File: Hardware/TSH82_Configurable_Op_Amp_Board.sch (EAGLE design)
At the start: 33 parts, among them U1 TSH82

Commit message: Close to done, labels, layout, etc.
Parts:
- added FD1, FD2: FIDUCIAL1X2, SparkFun-Aesthetics:FIDUCIAL1X2
- added H1, H2: STAND-OFF, SparkFun-Hardware:STAND-OFF
- added LOGO1: SFE_LOGO_NAME_FLAME.2_INCH, SparkFun-Aesthetics:SFE_LOGO_NAME_FLAME.2_INCH
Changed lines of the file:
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@@
 <?xml version="1.0" encoding="utf-8"?>
 <!DOCTYPE eagle SYSTEM "eagle.dtd">
-<eagle version="9.0.1">
+<eagle version="9.1.0">
 <drawing>
 <settings>
@@
 <grid distance="0.1" unitdist="inch" unit="inch" style="lines" multiple="1" display="no" altdistance="0.01" altunitdist="inch" altunit="inch"/>
 <layers>
-<layer number="1" name="Top" color="4" fill="1" visible="yes" active="no"/>
-<layer number="2" name="Route2" color="1" fill="3" visible="yes" active="no"/>
-<layer number="15" name="Route15" color="4" fill="6" visible="yes" active="no"/>
-<layer number="16" name="Bottom" color="1" fill="1" visible="yes" active="no"/>
-<layer number="17" name="Pads" color="2" fill="1" visible="yes" active="no"/>
-<layer number="18" name="Vias" color="2" fill="1" visible="yes" active="no"/>
-<layer number="19" name="Unrouted" color="6" fill="1" visible="yes" active="no"/>
-<layer number="20" name="Dimension" color="15" fill="1" visible="yes" active="no"/>
-<layer number="21" name="tPlace" color="16" fill="1" visible="yes" active="no"/>
-<layer number="22" name="bPlace" color="14" fill="1" visible="yes" active="no"/>
-<layer number="23" name="tOrigins" color="15" fill="1" visible="yes" active="no"/>
-<layer number="24" name="bOrigins" color="15" fill="1" visible="yes" active="no"/>
-<layer number="25" name="tNames" color="7" fill="1" visible="yes" active="no"/>
-<layer number="26" name="bNames" color="7" fill="1" visible="yes" active="no"/>
-<layer number="27" name="tValues" color="7" fill="1" visible="yes" active="no"/>
-<layer number="28" name="bValues" color="7" fill="1" visible="yes" active="no"/>
+<layer number="1" name="Top" color="4" fill="1" visible="no" active="no"/>
+<layer number="2" name="Route2" color="1" fill="3" visible="no" active="no"/>
+<layer number="15" name="Route15" color="4" fill="6" visible="no" active="no"/>
+<layer number="16" name="Bottom" color="1" fill="1" visible="no" active="no"/>
+<layer number="17" name="Pads" color="2" fill="1" visible="no" active="no"/>
+<layer number="18" name="Vias" color="2" fill="1" visible="no" active="no"/>
+<layer number="19" name="Unrouted" color="6" fill="1" visible="no" active="no"/>
+<layer number="20" name="Dimension" color="15" fill="1" visible="no" active="no"/>
+<layer number="21" name="tPlace" color="16" fill="1" visible="no" active="no"/>
+<layer number="22" name="bPlace" color="14" fill="1" visible="no" active="no"/>
+<layer number="23" name="tOrigins" color="15" fill="1" visible="no" active="no"/>
+<layer number="24" name="bOrigins" color="15" fill="1" visible="no" active="no"/>
+<layer number="25" name="tNames" color="7" fill="1" visible="no" active="no"/>
+<layer number="26" name="bNames" color="7" fill="1" visible="no" active="no"/>
+<layer number="27" name="tValues" color="7" fill="1" visible="no" active="no"/>
+<layer number="28" name="bValues" color="7" fill="1" visible="no" active="no"/>
 <layer number="29" name="tStop" color="7" fill="3" visible="no" active="no"/>
 <layer number="30" name="bStop" color="7" fill="6" visible="no" active="no"/>
@@
 <layer number="35" name="tGlue" color="7" fill="4" visible="no" active="no"/>
 <layer number="36" name="bGlue" color="7" fill="5" visible="no" active="no"/>
-<layer number="37" name="tTest" color="7" fill="1" visible="yes" active="no"/>
-<layer number="38" name="bTest" color="7" fill="1" visible="yes" active="no"/>
+<layer number="37" name="tTest" color="7" fill="1" visible="no" active="no"/>
+<layer number="38" name="bTest" color="7" fill="1" visible="no" active="no"/>
 <layer number="39" name="tKeepout" color="4" fill="11" visible="no" active="no"/>
 <layer number="40" name="bKeepout" color="1" fill="11" visible="no" active="no"/>
@@
 <layer number="44" name="Drills" color="7" fill="1" visible="no" active="no"/>
 <layer number="45" name="Holes" color="7" fill="1" visible="no" active="no"/>
-<layer number="46" name="Milling" color="3" fill="1" visible="yes" active="no"/>
-<layer number="47" name="Measures" color="7" fill="1" visible="yes" active="no"/>
-<layer number="48" name="Document" color="7" fill="1" visible="yes" active="no"/>
-<layer number="49" name="Reference" color="7" fill="1" visible="yes" active="no"/>
-<layer number="50" name="dxf" color="7" fill="1" visible="yes" active="no"/>
-<layer number="51" name="tDocu" color="6" fill="1" visible="yes" active="no"/>
-<layer number="52" name="bDocu" color="7" fill="1" visible="yes" active="no"/>
-<layer number="53" name="tGND_GNDA" color="7" fill="9" visible="yes" active="no"/>
-<layer number="54" name="bGND_GNDA" color="1" fill="9" visible="yes" active="no"/>
-<layer number="56" name="wert" color="7" fill="1" visible="yes" active="no"/>
-<layer number="57" name="tCAD" color="7" fill="1" visible="yes" active="no"/>
-<layer number="59" name="tCarbon" color="7" fill="1" visible="yes" active="no"/>
-<layer number="60" name="bCarbon" color="7" fill="1" visible="yes" active="no"/>
+<layer number="46" name="Milling" color="3" fill="1" visible="no" active="no"/>
+<layer number="47" name="Measures" color="7" fill="1" visible="no" active="no"/>
+<layer number="48" name="Document" color="7" fill="1" visible="no" active="no"/>
+<layer number="49" name="Reference" color="7" fill="1" visible="no" active="no"/>
+<layer number="50" name="dxf" color="7" fill="1" visible="no" active="no"/>
+<layer number="51" name="tDocu" color="6" fill="1" visible="no" active="no"/>
+<layer number="52" name="bDocu" color="7" fill="1" visible="no" active="no"/>
+<layer number="53" name="tGND_GNDA" color="7" fill="9" visible="no" active="no"/>
+<layer number="54" name="bGND_GNDA" color="1" fill="9" visible="no" active="no"/>
+<layer number="56" name="wert" color="7" fill="1" visible="no" active="no"/>
+<layer number="57" name="tCAD" color="7" fill="1" visible="no" active="no"/>
+<layer number="59" name="tCarbon" color="7" fill="1" visible="no" active="no"/>
+<layer number="60" name="bCarbon" color="7" fill="1" visible="no" active="no"/>
 <layer number="88" name="SimResults" color="9" fill="1" visible="yes" active="yes"/>
 <layer number="89" name="SimProbes" color="9" fill="1" visible="yes" active="yes"/>
@@
 <part name="C3" library="SparkFun-Capacitors" deviceset="10UF-POLAR" device="-EIA3216-16V-10%(TANT)" value="10uF"/>
 <part name="C10" library="SparkFun-Capacitors" deviceset="0.1UF" device="-0603-25V-(+80/-20%)" value="0.1uF"/>
+<part name="LOGO1" library="SparkFun-Aesthetics" deviceset="SFE_LOGO_NAME_FLAME" device=".2_INCH"/>
+<part name="H1" library="SparkFun-Hardware" deviceset="STAND-OFF" device=""/>
+<part name="H2" library="SparkFun-Hardware" deviceset="STAND-OFF" device=""/>
+<part name="FD1" library="SparkFun-Aesthetics" deviceset="FIDUCIAL" device="1X2"/>
+<part name="FD2" library="SparkFun-Aesthetics" deviceset="FIDUCIAL" device="1X2"/>
 </parts>
 <sheets>
@@
 <instance part="C3" gate="G$1" x="106.68" y="45.72"/>
 <instance part="C10" gate="G$1" x="119.38" y="43.18"/>
+<instance part="LOGO1" gate="G$1" x="167.64" y="48.26"/>
+<instance part="H1" gate="G$1" x="233.68" y="40.64"/>
+<instance part="H2" gate="G$1" x="238.76" y="40.64"/>
+<instance part="FD1" gate="G$1" x="228.6" y="40.64"/>
+<instance part="FD2" gate="G$1" x="223.52" y="40.64"/>
 </instances>
 <busses>

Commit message: Ready for review.
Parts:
- removed FD1, FD2: FIDUCIAL1X2, SparkFun-Aesthetics:FIDUCIAL1X2
- added LOGO2: SFE_LOGO_NAME_FLAME.1_INCH, SparkFun-Aesthetics:SFE_LOGO_NAME_FLAME.1_INCH
- added LOGO3: OSHW-LOGOS, SparkFun-Aesthetics:OSHW-LOGOS
- LOGO1: value SFE_LOGO_NAME_FLAME.2_INCH -> SFE_LOGO_FLAME.2_INCH; device SparkFun-Aesthetics:SFE_LOGO_NAME_FLAME.2_INCH -> SparkFun-Aesthetics:SFE_LOGO_FLAME.2_INCH
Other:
- note added: "+VCC - (-VEE) = 4.5V-12V"
- note added: "v01"
- moved on the sheet: C1, C2, R1, R2
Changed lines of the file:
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@@
 <part name="C3" library="SparkFun-Capacitors" deviceset="10UF-POLAR" device="-EIA3216-16V-10%(TANT)" value="10uF"/>
 <part name="C10" library="SparkFun-Capacitors" deviceset="0.1UF" device="-0603-25V-(+80/-20%)" value="0.1uF"/>
-<part name="LOGO1" library="SparkFun-Aesthetics" deviceset="SFE_LOGO_NAME_FLAME" device=".2_INCH"/>
 <part name="H1" library="SparkFun-Hardware" deviceset="STAND-OFF" device=""/>
 <part name="H2" library="SparkFun-Hardware" deviceset="STAND-OFF" device=""/>
-<part name="FD1" library="SparkFun-Aesthetics" deviceset="FIDUCIAL" device="1X2"/>
-<part name="FD2" library="SparkFun-Aesthetics" deviceset="FIDUCIAL" device="1X2"/>
+<part name="LOGO1" library="SparkFun-Aesthetics" deviceset="SFE_LOGO_FLAME" device=".2_INCH"/>
+<part name="LOGO2" library="SparkFun-Aesthetics" deviceset="SFE_LOGO_NAME_FLAME" device=".1_INCH"/>
+<part name="LOGO3" library="SparkFun-Aesthetics" deviceset="OSHW-LOGO" device="S"/>
 </parts>
 <sheets>
@@
 <wire x1="0" y1="81.28" x2="124.46" y2="81.28" width="0.1524" layer="97" style="shortdash"/>
 <wire x1="124.46" y1="81.28" x2="147.32" y2="81.28" width="0.1524" layer="97" style="shortdash"/>
-<wire x1="147.32" y1="81.28" x2="248.92" y2="81.28" width="0.1524" layer="97" style="shortdash"/>
 <wire x1="124.46" y1="185.42" x2="124.46" y2="81.28" width="0.1524" layer="97" style="shortdash"/>
 <wire x1="147.32" y1="35.56" x2="147.32" y2="81.28" width="0.1524" layer="97" style="shortdash"/>
@@
 <text x="20.32" y="20.32" size="2.54" layer="94" font="vector">Connector</text>
 <text x="81.28" y="15.24" size="2.54" layer="94" font="vector">Power and Reference</text>
+<text x="238.76" y="7.62" size="2.54" layer="94">v01</text>
+<text x="9.144" y="14.478" size="2.54" layer="94" font="vector">+VCC - (-VEE) = 4.5V-12V</text>
 </plain>
 <instances>
@@
 <instance part="FRAME1" gate="G$1" x="0" y="0"/>
 <instance part="FRAME1" gate="V" x="147.32" y="0"/>
-<instance part="R1" gate="G$1" x="68.58" y="53.34" smashed="yes" rot="R90">
-<attribute name="NAME" x="67.056" y="53.34" size="1.778" layer="95" font="vector" rot="R90" align="bottom-center"/>
-<attribute name="VALUE" x="70.104" y="53.34" size="1.778" layer="96" font="vector" rot="R90" align="top-center"/>
-</instance>
-<instance part="R2" gate="G$1" x="68.58" y="38.1" smashed="yes" rot="R90">
-<attribute name="NAME" x="67.056" y="38.1" size="1.778" layer="95" font="vector" rot="R90" align="bottom-center"/>
-<attribute name="VALUE" x="70.104" y="38.1" size="1.778" layer="96" font="vector" rot="R90" align="top-center"/>
-</instance>
-<instance part="C2" gate="G$1" x="93.98" y="35.56" smashed="yes">
-<attribute name="NAME" x="95.504" y="38.481" size="1.778" layer="95" font="vector"/>
-<attribute name="VALUE" x="95.504" y="33.401" size="1.778" layer="96" font="vector"/>
+<instance part="R1" gate="G$1" x="60.96" y="53.34" smashed="yes" rot="R90">
+<attribute name="NAME" x="59.436" y="53.34" size="1.778" layer="95" font="vector" rot="R90" align="bottom-center"/>
+<attribute name="VALUE" x="62.484" y="53.34" size="1.778" layer="96" font="vector" rot="R90" align="top-center"/>
+</instance>
+<instance part="R2" gate="G$1" x="60.96" y="38.1" smashed="yes" rot="R90">
+<attribute name="NAME" x="59.436" y="38.1" size="1.778" layer="95" font="vector" rot="R90" align="bottom-center"/>
+<attribute name="VALUE" x="62.484" y="38.1" size="1.778" layer="96" font="vector" rot="R90" align="top-center"/>
+</instance>
+<instance part="C2" gate="G$1" x="86.36" y="35.56" smashed="yes">
+<attribute name="NAME" x="87.884" y="38.481" size="1.778" layer="95" font="vector"/>
+<attribute name="VALUE" x="87.884" y="33.401" size="1.778" layer="96" font="vector"/>
 </instance>
 <instance part="-VEE" gate="G$2" x="99.06" y="25.4" smashed="yes">
@@
 <attribute name="NAME" x="198.12" y="116.84" size="1.778" layer="95" font="vector" rot="R270"/>
 </instance>
-<instance part="C1" gate="G$1" x="81.28" y="38.1"/>
+<instance part="C1" gate="G$1" x="73.66" y="38.1"/>
 <instance part="C3" gate="G$1" x="106.68" y="45.72"/>
 <instance part="C10" gate="G$1" x="119.38" y="43.18"/>
-<instance part="LOGO1" gate="G$1" x="167.64" y="48.26"/>
-<instance part="H1" gate="G$1" x="233.68" y="40.64"/>
-<instance part="H2" gate="G$1" x="238.76" y="40.64"/>
-<instance part="FD1" gate="G$1" x="228.6" y="40.64"/>
-<instance part="FD2" gate="G$1" x="223.52" y="40.64"/>
+<instance part="H1" gate="G$1" x="241.808" y="40.894"/>
+<instance part="H2" gate="G$1" x="245.618" y="40.894"/>
+<instance part="LOGO1" gate="G$1" x="182.626" y="48.26"/>
+<instance part="LOGO2" gate="G$1" x="150.114" y="35.814"/>
+<instance part="LOGO3" gate="G$1" x="223.012" y="49.022"/>
 </instances>
 <busses>
@@
 <pinref part="R1" gate="G$1" pin="1"/>
 <pinref part="R2" gate="G$1" pin="2"/>
-<wire x1="68.58" y1="48.26" x2="68.58" y2="45.72" width="0.1524" layer="91"/>
-<wire x1="68.58" y1="45.72" x2="68.58" y2="43.18" width="0.1524" layer="91"/>
-<wire x1="81.28" y1="40.64" x2="81.28" y2="45.72" width="0.1524" layer="91"/>
-<wire x1="81.28" y1="45.72" x2="68.58" y2="45.72" width="0.1524" layer="91"/>
+<wire x1="60.96" y1="48.26" x2="60.96" y2="45.72" width="0.1524" layer="91"/>
+<wire x1="60.96" y1="45.72" x2="60.96" y2="43.18" width="0.1524" layer="91"/>
+<wire x1="73.66" y1="40.64" x2="73.66" y2="45.72" width="0.1524" layer="91"/>
+<wire x1="73.66" y1="45.72" x2="60.96" y2="45.72" width="0.1524" layer="91"/>
 <pinref part="C2" gate="G$1" pin="1"/>
-<wire x1="93.98" y1="40.64" x2="93.98" y2="45.72" width="0.1524" layer="91"/>
-<wire x1="93.98" y1="45.72" x2="81.28" y2="45.72" width="0.1524" layer="91"/>
-<junction x="68.58" y="45.72"/>
-<junction x="81.28" y="45.72"/>
-<label x="60.96" y="45.72" size="1.778" layer="95" rot="R180" xref="yes"/>
-<wire x1="60.96" y1="45.72" x2="68.58" y2="45.72" width="0.1524" layer="91"/>
+<wire x1="86.36" y1="40.64" x2="86.36" y2="45.72" width="0.1524" layer="91"/>
+<wire x1="86.36" y1="45.72" x2="73.66" y2="45.72" width="0.1524" layer="91"/>
+<junction x="60.96" y="45.72"/>
+<junction x="73.66" y="45.72"/>
+<label x="91.44" y="45.72" size="1.778" layer="95" xref="yes"/>
 <pinref part="C1" gate="G$1" pin="+"/>
+<wire x1="86.36" y1="45.72" x2="91.44" y2="45.72" width="0.1524" layer="91"/>
 </segment>
 <segment>
@@
 <segment>
 <pinref part="R2" gate="G$1" pin="1"/>
-<wire x1="68.58" y1="33.02" x2="68.58" y2="30.48" width="0.1524" layer="91"/>
-<wire x1="68.58" y1="30.48" x2="81.28" y2="30.48" width="0.1524" layer="91"/>
-<wire x1="81.28" y1="30.48" x2="93.98" y2="30.48" width="0.1524" layer="91"/>
-<wire x1="93.98" y1="30.48" x2="99.06" y2="30.48" width="0.1524" layer="91"/>
+<wire x1="60.96" y1="33.02" x2="60.96" y2="30.48" width="0.1524" layer="91"/>
+<wire x1="60.96" y1="30.48" x2="73.66" y2="30.48" width="0.1524" layer="91"/>
+<wire x1="73.66" y1="30.48" x2="86.36" y2="30.48" width="0.1524" layer="91"/>
+<wire x1="86.36" y1="30.48" x2="99.06" y2="30.48" width="0.1524" layer="91"/>
 <wire x1="99.06" y1="30.48" x2="106.68" y2="30.48" width="0.1524" layer="91"/>
 <wire x1="106.68" y1="30.48" x2="106.68" y2="40.64" width="0.1524" layer="91"/>
-<wire x1="81.28" y1="33.02" x2="81.28" y2="30.48" width="0.1524" layer="91"/>
+<wire x1="73.66" y1="33.02" x2="73.66" y2="30.48" width="0.1524" layer="91"/>
 <pinref part="C2" gate="G$1" pin="2"/>
-<wire x1="93.98" y1="33.02" x2="93.98" y2="30.48" width="0.1524" layer="91"/>
-<junction x="93.98" y="30.48"/>
-<junction x="81.28" y="30.48"/>
+<wire x1="86.36" y1="33.02" x2="86.36" y2="30.48" width="0.1524" layer="91"/>
+<junction x="86.36" y="30.48"/>
+<junction x="73.66" y="30.48"/>
 <wire x1="132.08" y1="35.56" x2="132.08" y2="30.48" width="0.1524" layer="91"/>
 <wire x1="132.08" y1="30.48" x2="119.38" y2="30.48" width="0.1524" layer="91"/>
@@
 <segment>
 <pinref part="R1" gate="G$1" pin="2"/>
-<wire x1="68.58" y1="58.42" x2="68.58" y2="60.96" width="0.1524" layer="91"/>
-<wire x1="68.58" y1="60.96" x2="99.06" y2="60.96" width="0.1524" layer="91"/>
+<wire x1="60.96" y1="58.42" x2="60.96" y2="60.96" width="0.1524" layer="91"/>
+<wire x1="60.96" y1="60.96" x2="99.06" y2="60.96" width="0.1524" layer="91"/>
 <wire x1="99.06" y1="60.96" x2="106.68" y2="60.96" width="0.1524" layer="91"/>
 <wire x1="106.68" y1="60.96" x2="106.68" y2="48.26" width="0.1524" layer="91"/>

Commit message: Changes post design review.
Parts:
- added FD1, FD2: FIDUCIALUFIDUCIAL, SparkFun-Aesthetics:FIDUCIALUFIDUCIAL
- J1: device SparkFun-Connectors:CONN_09 -> SparkFun-Connectors:CONN_09NO_SILK
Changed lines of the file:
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@@
 <layer number="18" name="Vias" color="2" fill="1" visible="no" active="no"/>
 <layer number="19" name="Unrouted" color="6" fill="1" visible="no" active="no"/>
-<layer number="20" name="Dimension" color="15" fill="1" visible="no" active="no"/>
-<layer number="21" name="tPlace" color="16" fill="1" visible="no" active="no"/>
-<layer number="22" name="bPlace" color="14" fill="1" visible="no" active="no"/>
+<layer number="20" name="Dimension" color="24" fill="1" visible="no" active="no"/>
+<layer number="21" name="tPlace" color="7" fill="1" visible="no" active="no"/>
+<layer number="22" name="bPlace" color="7" fill="1" visible="no" active="no"/>
 <layer number="23" name="tOrigins" color="15" fill="1" visible="no" active="no"/>
 <layer number="24" name="bOrigins" color="15" fill="1" visible="no" active="no"/>
@@
 <layer number="49" name="Reference" color="7" fill="1" visible="no" active="no"/>
 <layer number="50" name="dxf" color="7" fill="1" visible="no" active="no"/>
-<layer number="51" name="tDocu" color="6" fill="1" visible="no" active="no"/>
+<layer number="51" name="tDocu" color="7" fill="1" visible="no" active="no"/>
 <layer number="52" name="bDocu" color="7" fill="1" visible="no" active="no"/>
 <layer number="53" name="tGND_GNDA" color="7" fill="9" visible="no" active="no"/>
@@
 </classes>
 <parts>
-<part name="J1" library="SparkFun-Connectors" deviceset="CONN_09" device=""/>
+<part name="J1" library="SparkFun-Connectors" deviceset="CONN_09" device="NO_SILK"/>
 <part name="FRAME1" library="SparkFun-Aesthetics" deviceset="FRAME-LETTER" device=""/>
 <part name="R1" library="SparkFun-Resistors" deviceset="2.2KOHM" device="-0603-1/10W-1%" value="2.2k"/>
@@
 <part name="LOGO2" library="SparkFun-Aesthetics" deviceset="SFE_LOGO_NAME_FLAME" device=".1_INCH"/>
 <part name="LOGO3" library="SparkFun-Aesthetics" deviceset="OSHW-LOGO" device="S"/>
+<part name="FD1" library="SparkFun-Aesthetics" deviceset="FIDUCIAL" device="UFIDUCIAL"/>
+<part name="FD2" library="SparkFun-Aesthetics" deviceset="FIDUCIAL" device="UFIDUCIAL"/>
 </parts>
 <sheets>
@@
 <instance part="C3" gate="G$1" x="106.68" y="45.72"/>
 <instance part="C10" gate="G$1" x="119.38" y="43.18"/>
-<instance part="H1" gate="G$1" x="241.808" y="40.894"/>
-<instance part="H2" gate="G$1" x="245.618" y="40.894"/>
+<instance part="H1" gate="G$1" x="241.808" y="45.974"/>
+<instance part="H2" gate="G$1" x="245.618" y="45.974"/>
 <instance part="LOGO1" gate="G$1" x="182.626" y="48.26"/>
 <instance part="LOGO2" gate="G$1" x="150.114" y="35.814"/>
 <instance part="LOGO3" gate="G$1" x="223.012" y="49.022"/>
+<instance part="FD1" gate="G$1" x="241.808" y="42.418"/>
+<instance part="FD2" gate="G$1" x="245.618" y="42.418"/>
 </instances>
 <busses>
@@
 <pinref part="C1" gate="G$1" pin="+"/>
 <wire x1="86.36" y1="45.72" x2="91.44" y2="45.72" width="0.1524" layer="91"/>
+<junction x="86.36" y="45.72"/>
 </segment>
 <segment>
@@
 <wire x1="78.74" y1="157.48" x2="73.66" y2="157.48" width="0.1524" layer="91"/>
 <wire x1="73.66" y1="157.48" x2="73.66" y2="149.86" width="0.1524" layer="91"/>
+<junction x="73.66" y="149.86"/>
 </segment>
 </net>
@@
 <wire x1="93.98" y1="139.7" x2="101.6" y2="139.7" width="0.1524" layer="91"/>
 <label x="101.6" y="139.7" size="1.778" layer="95" xref="yes"/>
-</segment>
-<segment>
+<junction x="93.98" y="149.86"/>
+<junction x="93.98" y="139.7"/>
+</segment>
+<segment>

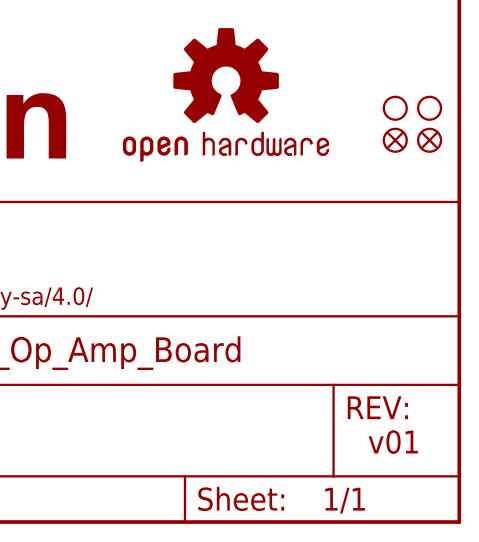
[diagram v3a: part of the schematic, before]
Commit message: Add bottom fiducials, move a trace, increment version, remove extra files.
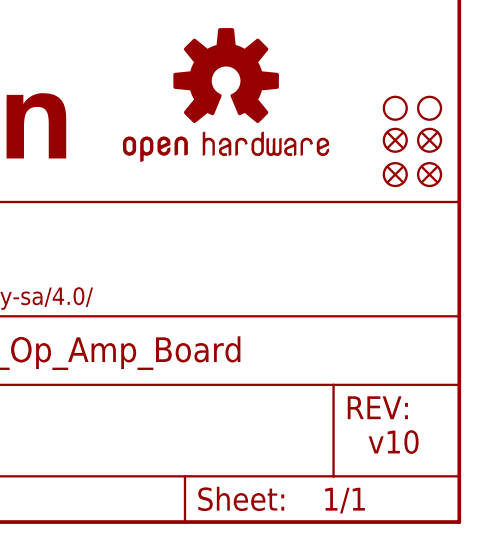
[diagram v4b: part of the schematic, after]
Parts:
- added FD3, FD4: FIDUCIALUFIDUCIAL, SparkFun-Aesthetics:FIDUCIALUFIDUCIAL
- U1: device pete:TSH82 -> SparkFun-IC-Amplifiers:TSH82
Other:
- note added: "v10"
- note removed: "v01"
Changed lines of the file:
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@@
 <part name="SUPPLY3" library="SparkFun-PowerSymbols" deviceset="VCC" device="" value="+VCC"/>
 <part name="SUPPLY4" library="SparkFun-PowerSymbols" deviceset="VNEG" device="" value="-VEE"/>
-<part name="U1" library="pete" deviceset="TSH82" device=""/>
+<part name="U1" library="SparkFun-IC-Amplifiers" deviceset="TSH82" device=""/>
 <part name="R3" library="SparkFun-Resistors" deviceset="10KOHM" device="-0603-1/10W-1%" value="10k"/>
 <part name="R4" library="SparkFun-Resistors" deviceset="10KOHM" device="-0603-1/10W-1%" value="10k"/>
@@
 <part name="FD1" library="SparkFun-Aesthetics" deviceset="FIDUCIAL" device="UFIDUCIAL"/>
 <part name="FD2" library="SparkFun-Aesthetics" deviceset="FIDUCIAL" device="UFIDUCIAL"/>
+<part name="FD3" library="SparkFun-Aesthetics" deviceset="FIDUCIAL" device="UFIDUCIAL"/>
+<part name="FD4" library="SparkFun-Aesthetics" deviceset="FIDUCIAL" device="UFIDUCIAL"/>
 </parts>
 <sheets>
@@
 <text x="20.32" y="20.32" size="2.54" layer="94" font="vector">Connector</text>
 <text x="81.28" y="15.24" size="2.54" layer="94" font="vector">Power and Reference</text>
-<text x="238.76" y="7.62" size="2.54" layer="94">v01</text>
+<text x="238.76" y="7.62" size="2.54" layer="94">v10</text>
 <text x="9.144" y="14.478" size="2.54" layer="94" font="vector">+VCC - (-VEE) = 4.5V-12V</text>
 </plain>
@@
 <instance part="FD1" gate="G$1" x="241.808" y="42.418"/>
 <instance part="FD2" gate="G$1" x="245.618" y="42.418"/>
+<instance part="FD3" gate="G$1" x="245.618" y="38.608"/>
+<instance part="FD4" gate="G$1" x="241.808" y="38.608"/>
 </instances>
 <busses>
